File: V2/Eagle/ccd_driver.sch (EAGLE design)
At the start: 63 parts, among them IC1 FT232RL, J2 USB-MINIB-5PIN, J3 POWER_JACK, Q2 BC214, U2 MK02FN128VLF10

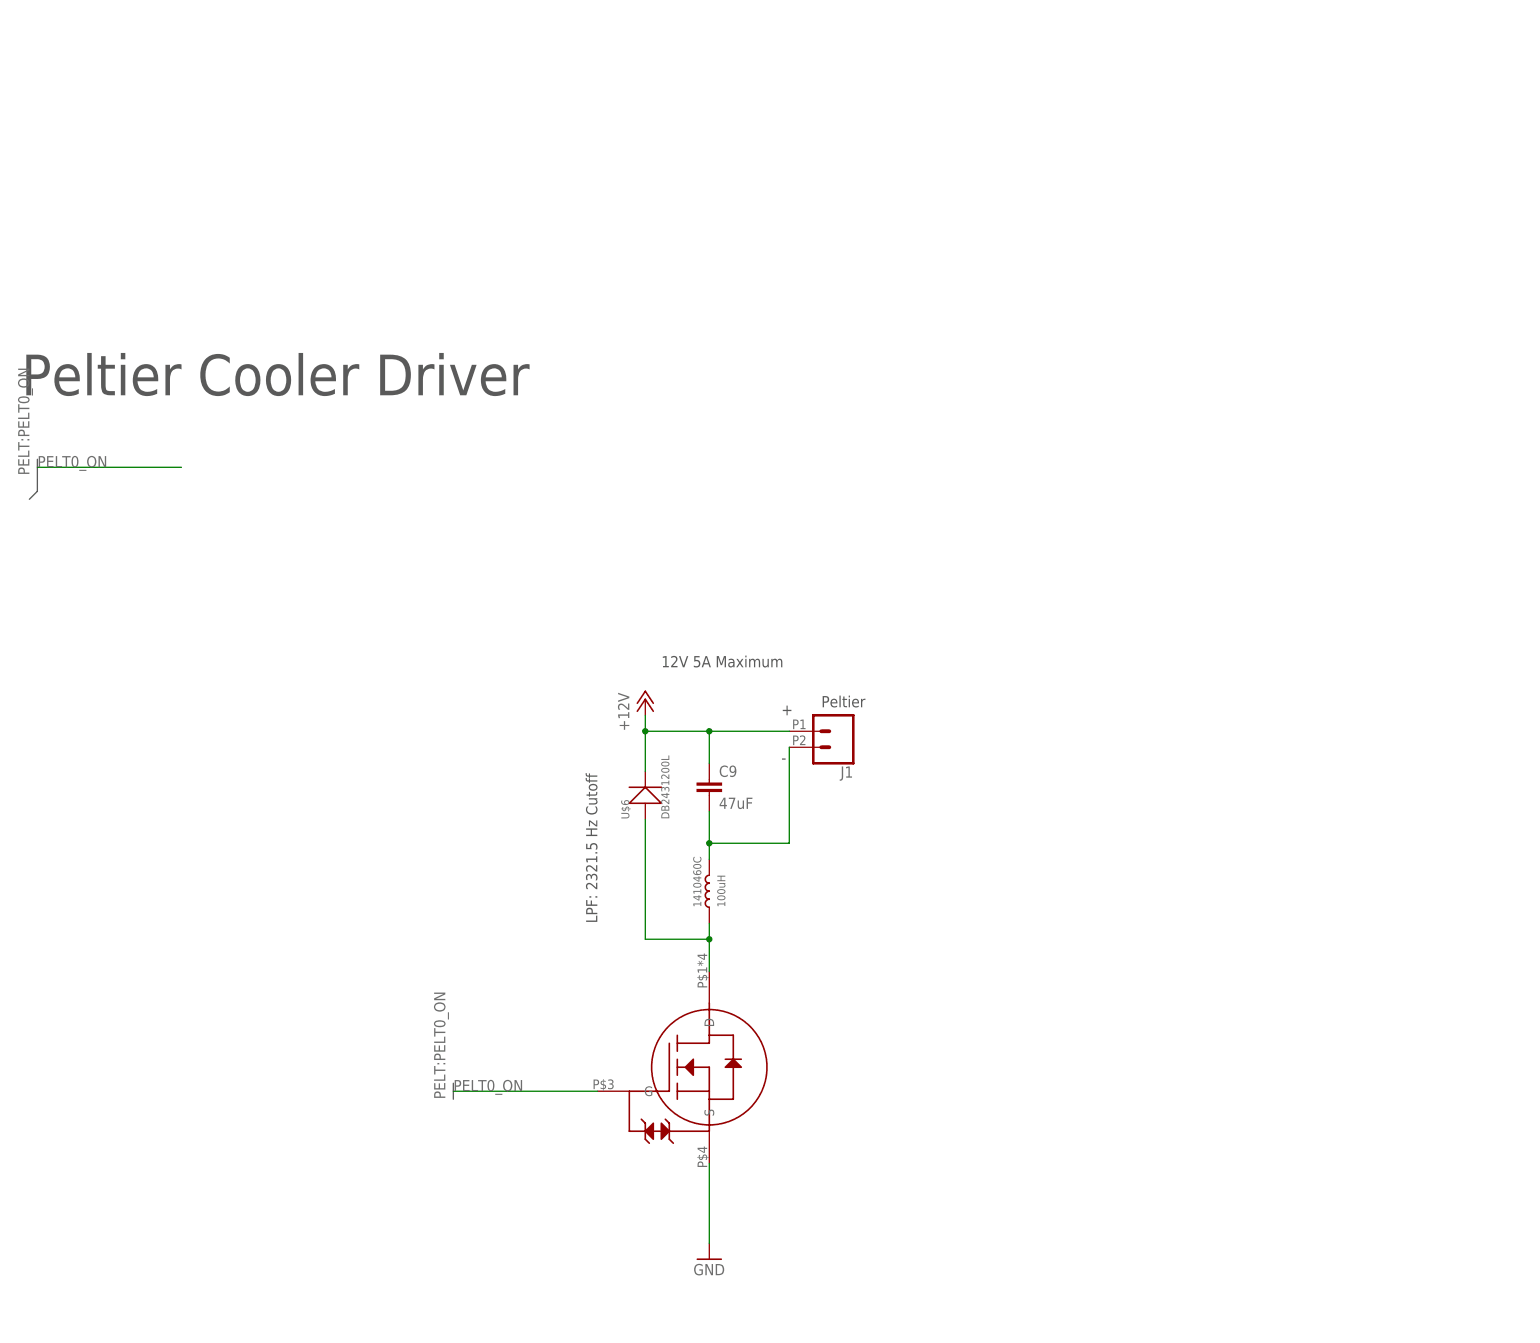
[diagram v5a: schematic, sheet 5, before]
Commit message: added fan mosfet control
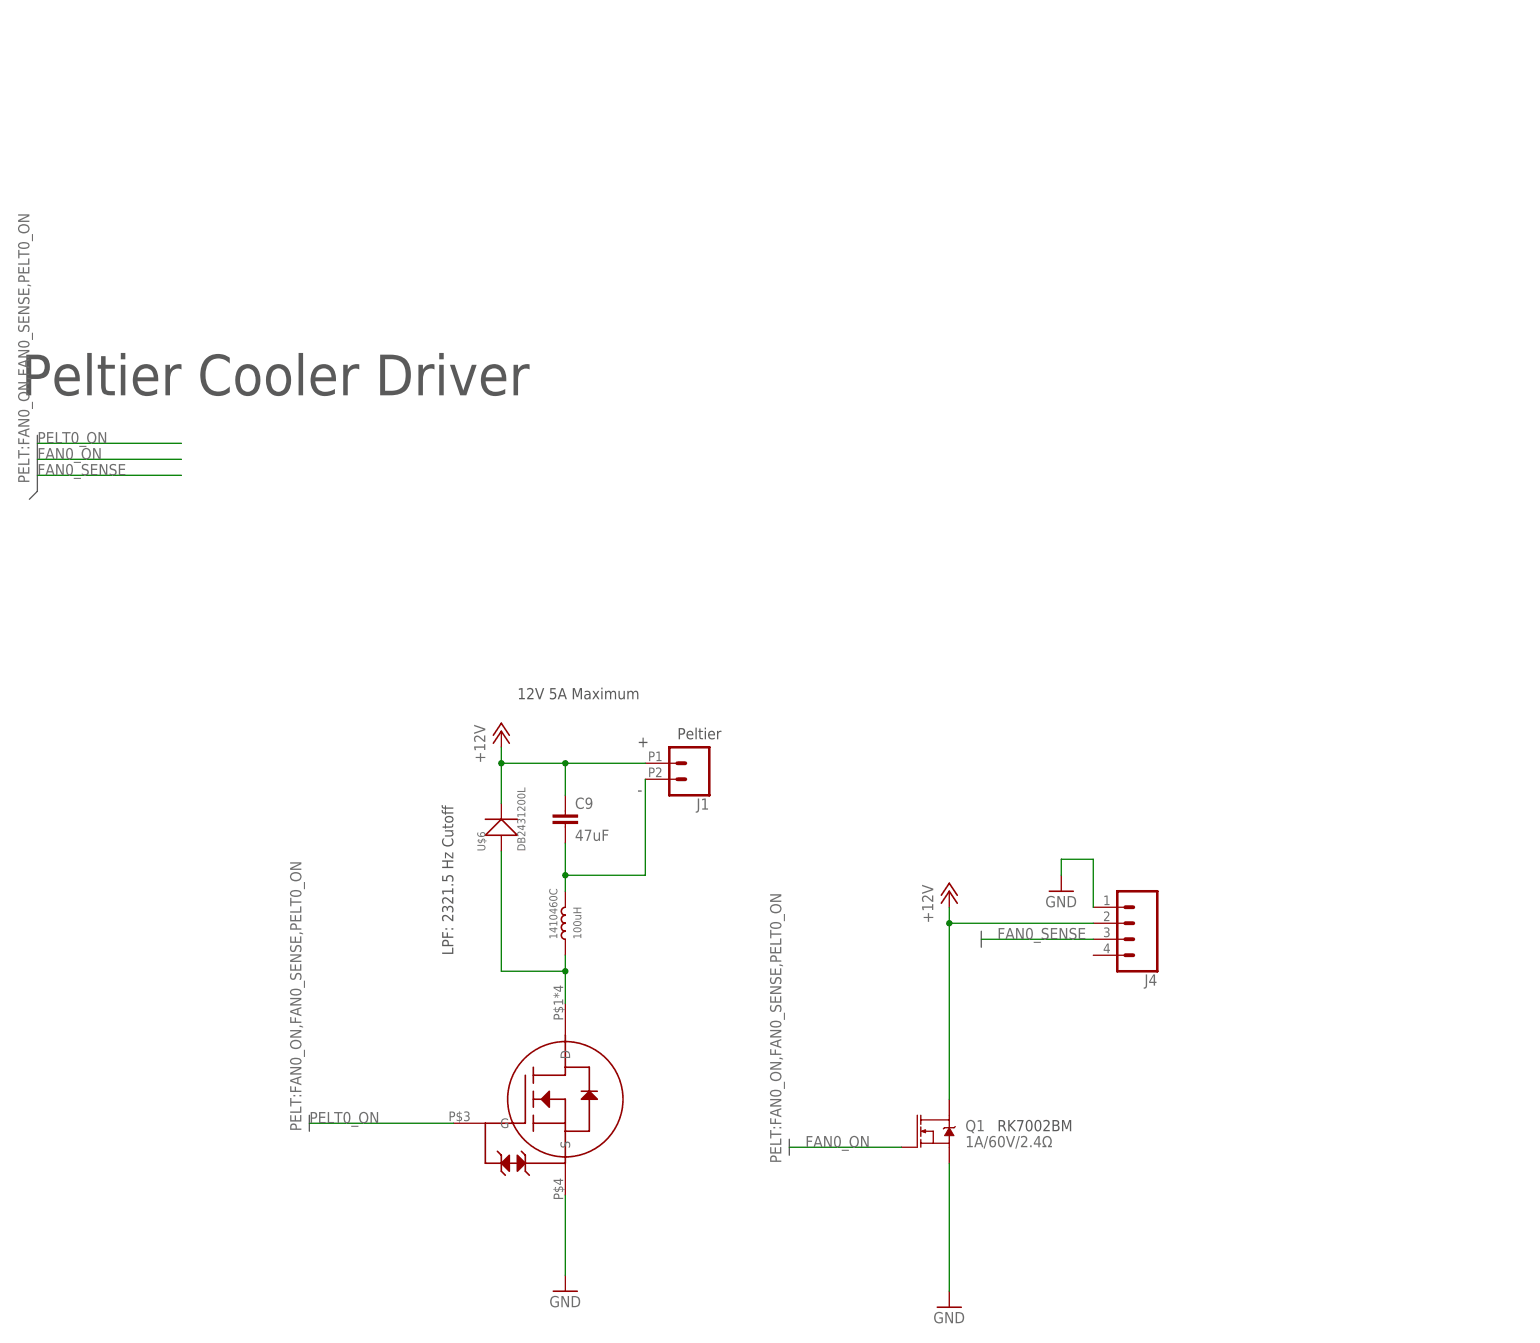
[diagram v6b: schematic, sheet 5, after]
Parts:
- added J4: (no value), SparkFun-Connectors:CONN_04JST-PTH
- added Q1: 1A/60V/2.4Ω, SparkFun-DiscreteSemi:MOSFET-NCH-BSS138
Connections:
- new net FAN0_ON: Q1.G
- new net FAN0_SENSE: J4.3
- net +12V: now also J4.2, Q1.D
- net GND: now also J4.1, Q1.S
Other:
- note added: "RK7002BM"
- note added: "TODO: Add motor control for fan [X]"
- note removed: "TODO: Add motor control for fan"
- moved on the sheet: 1410460C, C9, J1, U$6

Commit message: added different USB controller, micro usb, input protection
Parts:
- removed C15: 10uF, resistor:C-EUC1206
- removed C3: 0.1 µF, resistor:C-EUC1206
- removed IC1: FT232RL, ftdichip:FT232RL
- removed R1, R9: 22, resistor:R-US_R0805
- removed R10, R11: 1k, resistor:R-US_R0805
- removed RX_LED1, TX_LED1: (no value), led:LEDCHIPLED_0805
- removed TP4, TP5, TP6: TPPAD1-17Y, testpad:TPPAD1-17Y
- removed U$1: LD1117V33, ccd:LD1117V33
- added D13: TPD1E10B06DPYR, TPD1E10B06DPYR:TPD1E10B06DPYR
- added U10: TPD4S012DRYR, TPD4S012:TPD4S012DRYR
- added U11: 0ZCJ0050FF2G, 0ZCJ0050FF2G:0ZCJ0050FF2G
- added U5: CP2102N-A01-GQFN20R, CP2102N-A01-GQFN20R:CP2102N-A01-GQFN20R
- C1: value 0.1 µF -> 100nF; device resistor:C-EUC1206 -> SparkFun-Capacitors:10PF-50V-5%(0603)
- C2: value 0.1 µF -> 10uF; device resistor:C-EUC1206 -> SparkFun-Capacitors:10PF-50V-5%(0603)
- J2: value USB-MINIB-5PIN -> (none); device SparkFun-Connectors:USB-MINIB-5PIN -> SparkFun-Connectors:USB_MICRO-B_FEMALE-SMT
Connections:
- removed net N$1: IC1.USBDM, R1.1
- removed net N$10: R11.2, RX_LED1.C
- removed net N$2: IC1.USBDP, R9.1
- removed net N$24: R10.2, TX_LED1.C
- removed net N$3: J2.D-, R1.2
- removed net N$4: J2.D+, R9.2
- removed net N$5: C1.1, C2.2, IC1.3V3OUT, IC1.VCCIO
- removed net N$8: IC1.CBUS0, R10.1
- removed net N$9: IC1.CBUS1, R11.1
- new net CTS: U5.CTS
- new net D+: J2.D+, U10.D1+, U5.D+
- new net D-: J2.D-, U10.D-, U5.D-
- new net N$19: J2.VBUS, U11.2
- new net RTS: U5.RTS
- new net RX: U5.RXD
- new net TX: U5.TXD
- new net V_USB: C1.1, C2.1, D13.2, U10.VBUS, U11.1, U5.VBUS, U5.VREGIN
- net 3.3V: no longer C15.1, TP5.TP, U$1.VOUT
- net 5V: no longer C2.1, C3.1, IC1.!RESET, IC1.VCC, J2.VBUS, RX_LED1.A, TP4.TP, TX_LED1.A, U$1.VIN
- net GND: now also C2.2, D13.1, J2.SHIELD, U10.GND, U5.GND; no longer C15.2, C3.2, IC1.GND, IC1.GND@1, IC1.GND@2, IC1.GND@A, IC1.TEST, TP6.TP, U$1.GND
- net PCRX: no longer IC1.TXD
- net PCTX: no longer IC1.RXD
- net RESET: now also U5.RST
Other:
- note added: "Leave ID floating, type B device"

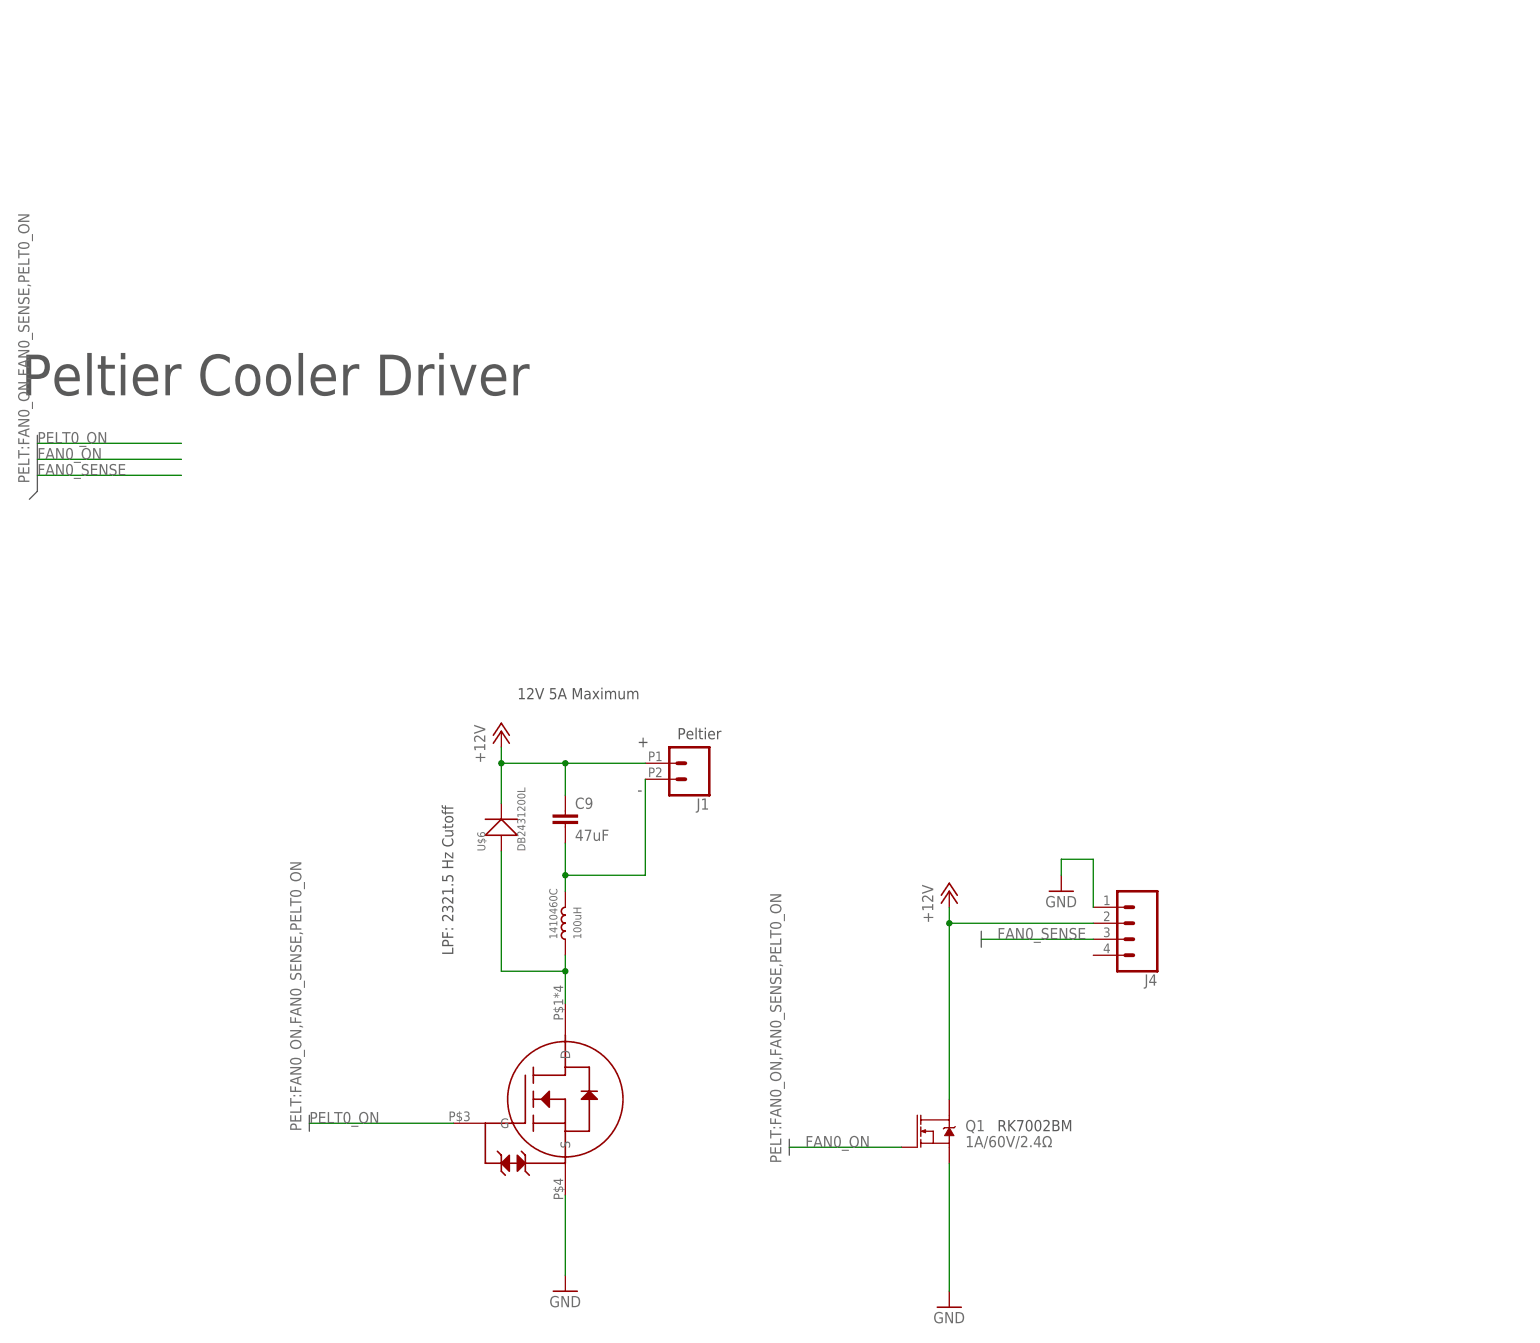
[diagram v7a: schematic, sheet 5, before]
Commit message: added thermistors
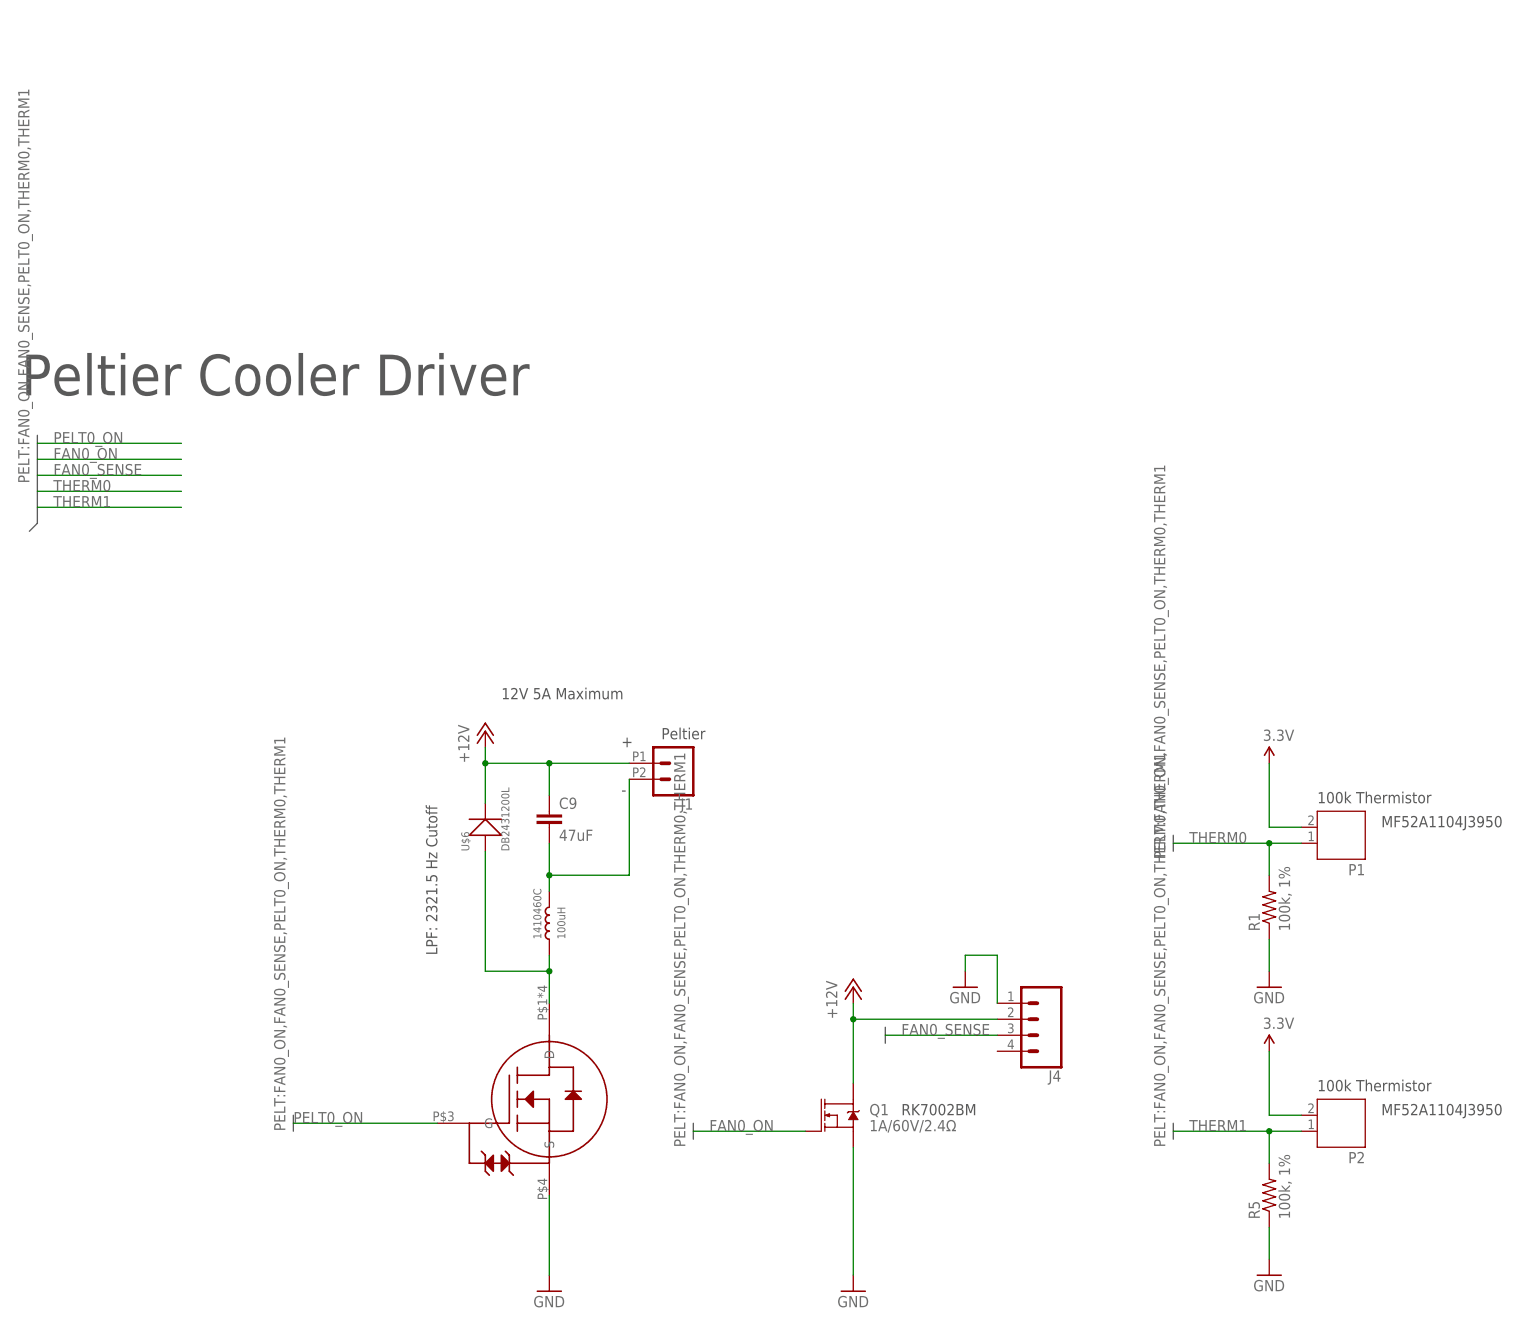
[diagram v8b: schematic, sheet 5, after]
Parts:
- added P1, P2: (no value), jst-ph:JST-PH2
- added R1, R5: 100k, 1%, audio amplifier example:R-US_R0603
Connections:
- new net THERM0: P1.1, R1.2
- new net THERM1: P2.1, R5.2
- net 3.3V: now also P1.2, P2.2
- net GND: now also R1.1, R5.1
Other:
- note added: "100k Thermistor"
- note added: "MF52A1104J3950"
- note added: "TODO: Change resistors to 0603"
- moved on the sheet: 1410460C, C9, J1, J4, Q1, U$6
